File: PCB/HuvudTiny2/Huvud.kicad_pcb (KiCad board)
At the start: 4 copper layers, 42 x 42 mm, 104 parts, among them J1 Vin, J12 USB_Micro-B, J2 DBG, J3 THERM, J4 FAN0, J5 FAN1, J6 Heater, J7 Endstop, J9 STEPPER, Q1 AO3400A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

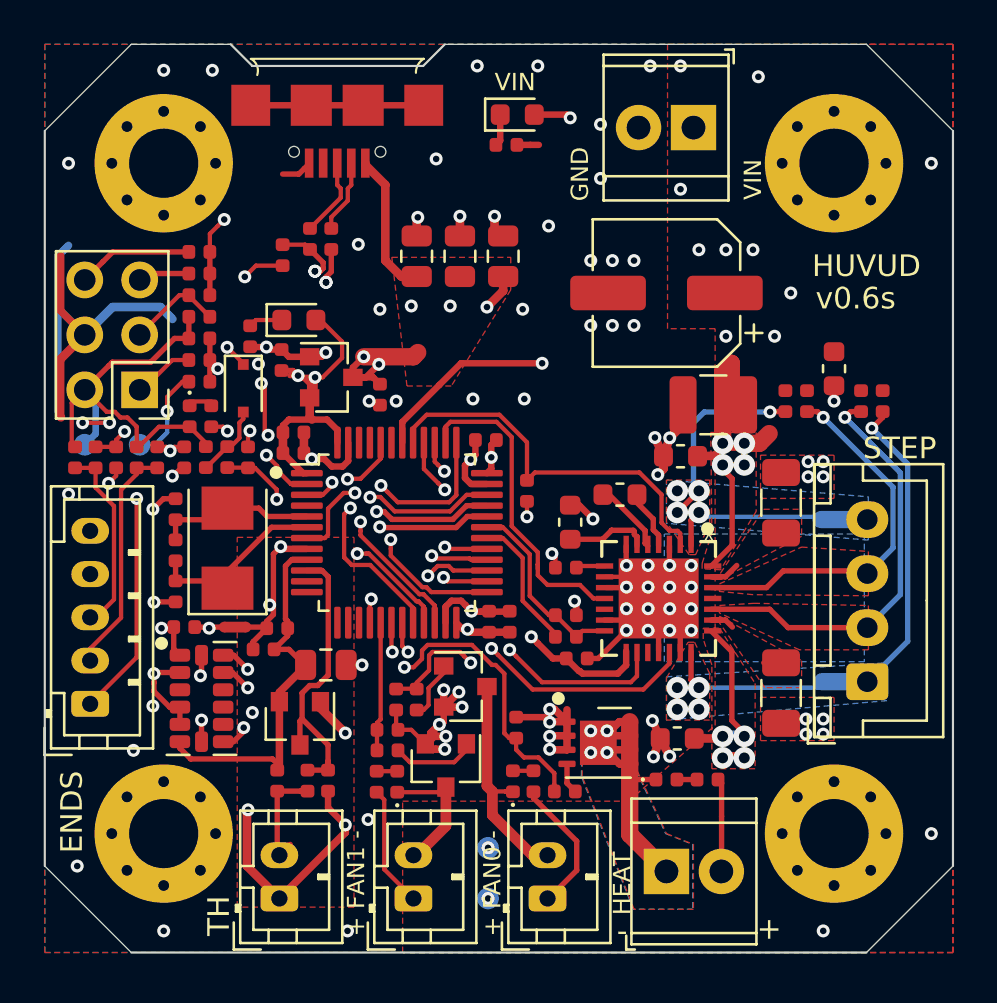
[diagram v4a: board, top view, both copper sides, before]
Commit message: Add caps across current sense resistors.
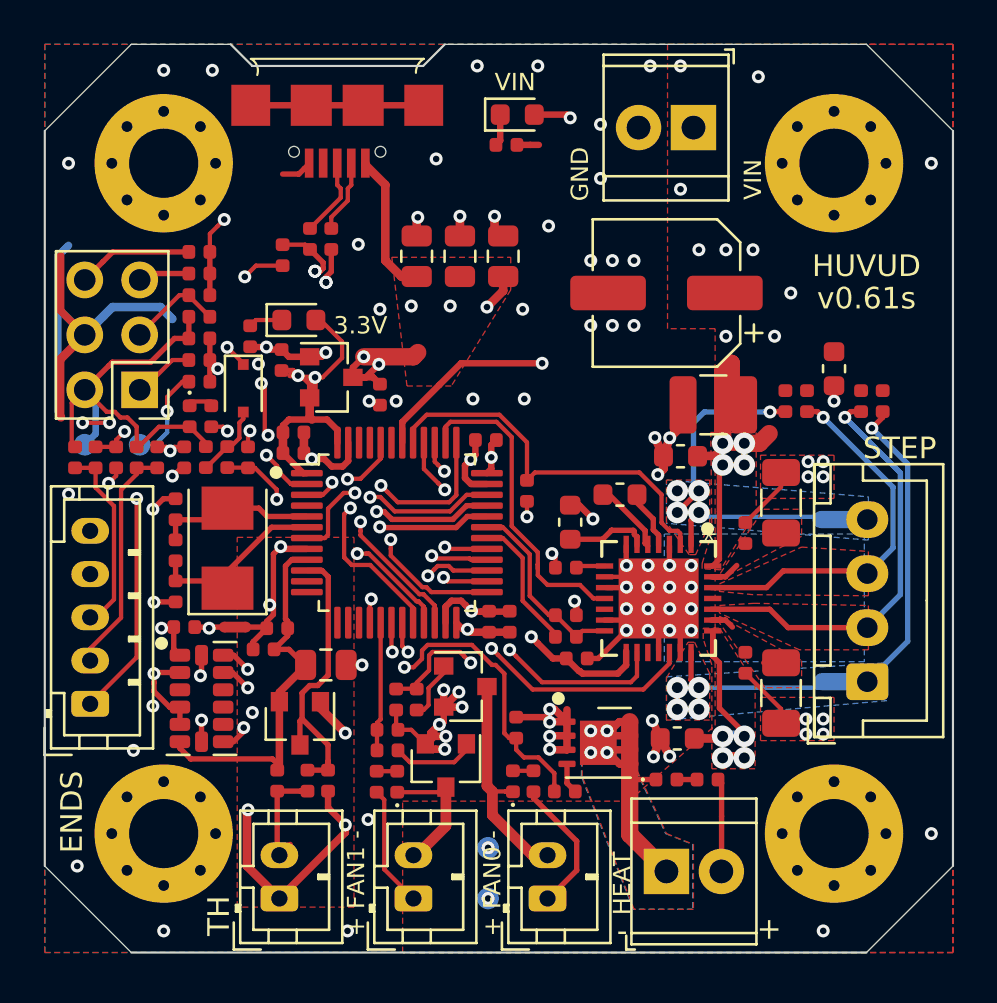
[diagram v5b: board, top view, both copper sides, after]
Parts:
- added C29: 100nF, Capacitor_SMD:C_0402_1005Metric, F.Cu at (214.4, 122.6)
- added C36: 100nF, Capacitor_SMD:C_0402_1005Metric, F.Cu at (214.4, 128.6)
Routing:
- net GND: track 118.2 -> 124.2 mm
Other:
- board text added: "3.3V"
- board text added: "v0.61s"
- board text removed: "v0.6s"

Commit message: Small tweaks to footprints.
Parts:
- C22: footprint Capacitor_SMD:C_1210_3225Metric -> Capacitor_SMD:C_1206_3216Metric
- Q3: value AON7524 -> AON7534
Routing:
- net ST_VS: track 46.1 -> 41.5 mm
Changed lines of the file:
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@@
       (effects (font (size 1 1) (thickness 0.15)))
     )
-    (fp_text value "AON7524" (at 0 2.45) (layer "F.Fab") hide
+    (fp_text value "AON7534" (at 0 2.45) (layer "F.Fab") hide
       (effects (font (size 1 1) (thickness 0.15)))
     )
@@
     )
   )
-  (footprint "Capacitor_SMD:C_1210_3225Metric" (layer "F.Cu")
+  (footprint "Capacitor_SMD:C_1206_3216Metric" (layer "F.Cu")
     (at 212.917103 116.672428)
-    (descr "Capacitor SMD 1210 (3225 Metric), square (rectangular) end terminal, IPC_7351 nominal, (Body size source: http://www.tortai-tech.com/upload/download/2011102023233369053.pdf), generated with kicad-footprint-generator")
+    (descr "Capacitor SMD 1206 (3216 Metric), square (rectangular) end terminal, IPC_7351 nominal, (Body size source: http://www.tortai-tech.com/upload/download/2011102023233369053.pdf), generated with kicad-footprint-generator")
     (tags "capacitor")
     (property "LCSC" "C13585")
@@
     (property "Sheetname" "")
     (attr smd)
-    (fp_text reference "C22" (at 0 -2.28) (layer "F.SilkS") hide
-      (effects (font (size 1 1) (thickness 0.15)))
-    )
-    (fp_text value "10uF/35V" (at 0 2.28) (layer "F.Fab") hide
+    (fp_text reference "C22" (at 0 -1.82) (layer "F.SilkS") hide
+      (effects (font (size 1 1) (thickness 0.15)))
+    )
+    (fp_text value "10uF/35V" (at 0 1.82) (layer "F.Fab")
       (effects (font (size 1 1) (thickness 0.15)))
     )
@@
       (effects (font (size 0.8 0.8) (thickness 0.12)))
     )
-    (fp_line (start -0.602064 -1.36) (end 0.602064 -1.36) (layer "F.SilkS") (width 0.12))
-    (fp_line (start -0.602064 1.36) (end 0.602064 1.36) (layer "F.SilkS") (width 0.12))
-    (fp_line (start -2.28 -1.58) (end 2.28 -1.58) (layer "F.CrtYd") (width 0.05))
-    (fp_line (start 2.28 -1.58) (end 2.28 1.58) (layer "F.CrtYd") (width 0.05))
-    (fp_line (start -2.28 1.58) (end -2.28 -1.58) (layer "F.CrtYd") (width 0.05))
-    (fp_line (start 2.28 1.58) (end -2.28 1.58) (layer "F.CrtYd") (width 0.05))
-    (fp_line (start 1.6 -1.25) (end 1.6 1.25) (layer "F.Fab") (width 0.1))
-    (fp_line (start 1.6 1.25) (end -1.6 1.25) (layer "F.Fab") (width 0.1))
-    (fp_line (start -1.6 1.25) (end -1.6 -1.25) (layer "F.Fab") (width 0.1))
-    (fp_line (start -1.6 -1.25) (end 1.6 -1.25) (layer "F.Fab") (width 0.1))
-    (pad "1" smd roundrect locked (at -1.4 0) (size 1.25 2.65) (layers "F.Cu" "F.Paste" "F.Mask") (roundrect_rratio 0.2)
+    (fp_line (start -0.602064 0.91) (end 0.602064 0.91) (layer "F.SilkS") (width 0.12))
+    (fp_line (start -0.602064 -0.91) (end 0.602064 -0.91) (layer "F.SilkS") (width 0.12))
+    (fp_line (start -2.28 -1.12) (end 2.28 -1.12) (layer "F.CrtYd") (width 0.05))
+    (fp_line (start 2.28 -1.12) (end 2.28 1.12) (layer "F.CrtYd") (width 0.05))
+    (fp_line (start 2.28 1.12) (end -2.28 1.12) (layer "F.CrtYd") (width 0.05))
+    (fp_line (start -2.28 1.12) (end -2.28 -1.12) (layer "F.CrtYd") (width 0.05))
+    (fp_line (start 1.6 -0.8) (end 1.6 0.8) (layer "F.Fab") (width 0.1))
+    (fp_line (start 1.6 0.8) (end -1.6 0.8) (layer "F.Fab") (width 0.1))
+    (fp_line (start -1.6 -0.8) (end 1.6 -0.8) (layer "F.Fab") (width 0.1))
+    (fp_line (start -1.6 0.8) (end -1.6 -0.8) (layer "F.Fab") (width 0.1))
+    (pad "1" smd roundrect locked (at -1.4 0) (size 1.25 1.75) (layers "F.Cu" "F.Paste" "F.Mask") (roundrect_rratio 0.2)
       (net 2 "GND") (pintype "passive"))
-    (pad "2" smd roundrect locked (at 1.4 0) (size 1.25 2.65) (layers "F.Cu" "F.Paste" "F.Mask") (roundrect_rratio 0.2)
+    (pad "2" smd roundrect locked (at 1.4 0) (size 1.25 1.75) (layers "F.Cu" "F.Paste" "F.Mask") (roundrect_rratio 0.2)
       (net 3 "ST_VS") (pintype "passive"))
-    (model "${KISYS3DMOD}/Capacitor_SMD.3dshapes/C_1210_3225Metric.wrl"
+    (model "${KISYS3DMOD}/Capacitor_SMD.3dshapes/C_1206_3216Metric.wrl"
       (offset (xyz 0 0 0))
       (scale (xyz 1 1 1))
@@
     (fp_line (start 0.5 0.25) (end -0.5 0.25) (layer "F.Fab") (width 0.1))
     (pad "1" smd roundrect locked (at -0.485 0 90) (size 0.59 0.64) (layers "F.Cu" "F.Paste" "F.Mask") (roundrect_rratio 0.25)
-      (net 32 "BRB"))
+      (net 32 "BRB") (pintype "passive"))
     (pad "2" smd roundrect locked (at 0.485 0 90) (size 0.59 0.64) (layers "F.Cu" "F.Paste" "F.Mask") (roundrect_rratio 0.25)
-      (net 2 "GND"))
+      (net 2 "GND") (pintype "passive"))
     (model "${KISYS3DMOD}/Capacitor_SMD.3dshapes/C_0402_1005Metric.wrl"
       (offset (xyz 0 0 0))
@@
   (segment (start 213.35 118.65) (end 213.025 119.025) (width 0.4) (layer "F.Cu") (net 3))
   (segment (start 213.35 132.85) (end 214.35 132.85) (width 0.25) (layer "F.Cu") (net 3))
-  (segment (start 213.35 115.15) (end 213.75 114.75) (width 0.8) (layer "F.Cu") (net 3))
   (segment (start 213.135 134) (end 213.3 134.165) (width 0.25) (layer "F.Cu") (net 3))
   (segment (start 213.025 119.025) (end 212.1875 119.05) (width 0.4) (layer "F.Cu") (net 3))
@@
   (segment (start 206.6 136.85) (end 206.6 138.2) (width 0.25) (layer "F.Cu") (net 3))
   (segment (start 212.8878 128.2878) (end 212.8878 127.1248) (width 0.25) (layer "F.Cu") (net 3))
-  (segment (start 213.35 118.45) (end 213.35 115.15) (width 0.8) (layer "F.Cu") (net 3))
   (segment (start 213.1 132.1) (end 213.35 131.85) (width 0.35) (layer "F.Cu") (net 3))
-  (segment (start 213.75 114.75) (end 213.75 115.5) (width 0.8) (layer "F.Cu") (net 3))
   (segment (start 206.6 138.2) (end 205.3 139.5) (width 0.25) (layer "F.Cu") (net 3))
   (segment (start 214.35 132.85) (end 214.35 131.85) (width 0.25) (layer "F.Cu") (net 3))
